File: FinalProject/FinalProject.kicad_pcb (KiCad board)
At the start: 4 copper layers, 100 x 100 mm, 143 parts, among them J1 GSB4111312HR, J10 Conn_01x02, J2 GSB4111312HR, J3 GSB4111312HR, J5 ARJM11D7-502-AB-EW2, J6 DCJ200-10-A-XX-K_REVA, J7 Conn_01x02, J9 Conn_01x03, Q1 NTTFS5C673NLTAG, Q2 NTTFS5C673NLTAG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

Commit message: having DRC error
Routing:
- net /DN1_D-: vias 1 -> 2
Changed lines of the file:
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@@
+	)
+	(via
+		(at 106.7 107.6)
+		(size 0.2)
+		(drill 0.1)
+		(layers "F.Cu" "B.Cu")
+		(net 101)
 	)
 	(via
@@
 	)
 	(segment
+		(start 81.0625 91)
+		(end 80.406249 91)
+		(width 0.2)
+		(layer "F.Cu")
+		(net 141)
+	)
+	(segment
 		(start 39.2125 67.05)
 		(end 39.2125 66.08)
@@
 		(start 39.2125 66.08)
 		(end 38.4125 65.28)
-		(width 0.2)
-		(layer "F.Cu")
-		(net 141)
-	)
-	(segment
-		(start 81.0625 91)
-		(end 80.406249 91)
 		(width 0.2)
 		(layer "F.Cu")
@@
 	)
 	(segment
+		(start 39.2125 68.245344)
+		(end 40.317156 69.35)
+		(width 0.2)
+		(layer "In2.Cu")
+		(net 141)
+	)
+	(segment
+		(start 68.517156 94)
+		(end 74.082844 94)
+		(width 0.2)
+		(layer "In2.Cu")
+		(net 141)
+	)
+	(segment
+		(start 77.132844 90.95)
+		(end 80.05 90.95)
+		(width 0.2)
+		(layer "In2.Cu")
+		(net 141)
+	)
+	(segment
+		(start 74.082844 94)
+		(end 77.132844 90.95)
+		(width 0.2)
+		(layer "In2.Cu")
+		(net 141)
+	)
+	(segment
+		(start 39.2125 67.05)
+		(end 39.2125 68.245344)
+		(width 0.2)
+		(layer "In2.Cu")
+		(net 141)
+	)
+	(segment
+		(start 43.867156 69.35)
+		(end 68.517156 94)
+		(width 0.2)
+		(layer "In2.Cu")
+		(net 141)
+	)
+	(segment
 		(start 40.317156 69.35)
-		(end 39.2125 68.245344)
-		(width 0.2)
-		(layer "In2.Cu")
-		(net 141)
-	)
-	(segment
-		(start 68.517156 94)
 		(end 43.867156 69.35)
-		(width 0.2)
-		(layer "In2.Cu")
-		(net 141)
-	)
-	(segment
-		(start 77.132844 90.95)
-		(end 74.082844 94)
-		(width 0.2)
-		(layer "In2.Cu")
-		(net 141)
-	)
-	(segment
-		(start 80.05 90.95)
-		(end 77.132844 90.95)
-		(width 0.2)
-		(layer "In2.Cu")
-		(net 141)
-	)
-	(segment
-		(start 74.082844 94)
-		(end 68.517156 94)
-		(width 0.2)
-		(layer "In2.Cu")
-		(net 141)
-	)
-	(segment
-		(start 39.2125 68.245344)
-		(end 39.2125 67.05)
-		(width 0.2)
-		(layer "In2.Cu")
-		(net 141)
-	)
-	(segment
-		(start 43.867156 69.35)
-		(end 40.317156 69.35)
 		(width 0.2)
 		(layer "In2.Cu")
@@
 	)
 	(segment
+		(start 45.2125 66.08)
+		(end 45.2125 67.05)
+		(width 0.2)
+		(layer "F.Cu")
+		(net 144)
+	)
+	(segment
 		(start 80.406249 89.5)
 		(end 80.356249 89.45)
@@
 	)
 	(segment
-		(start 45.2125 67.05)
+		(start 44.4125 65.28)
 		(end 45.2125 66.08)
-		(width 0.2)
-		(layer "F.Cu")
-		(net 144)
-	)
-	(segment
-		(start 45.2125 66.08)
-		(end 44.4125 65.28)
 		(width 0.2)
 		(layer "F.Cu")
@@
 	)
 	(segment
+		(start 79.182844 89.45)
+		(end 80.1 89.45)
+		(width 0.2)
+		(layer "In2.Cu")
+		(net 144)
+	)
+	(segment
+		(start 78.75413 89.878714)
+		(end 79.182844 89.45)
+		(width 0.2)
+		(layer "In2.Cu")
+		(net 144)
+	)
+	(segment
+		(start 77.49587 89.878714)
+		(end 78.75413 89.878714)
+		(width 0.2)
+		(layer "In2.Cu")
+		(net 144)
+	)
+	(segment
+		(start 73.667156 86.05)
+		(end 77.49587 89.878714)
+		(width 0.2)
+		(layer "In2.Cu")
+		(net 144)
+	)
+	(segment
 		(start 45.2125 67.545344)
 		(end 63.717156 86.05)
@@
 	)
 	(segment
-		(start 73.667156 86.05)
-		(end 77.49587 89.878714)
-		(width 0.2)
-		(layer "In2.Cu")
-		(net 144)
-	)
-	(segment
-		(start 78.75413 89.878714)
-		(end 79.182844 89.45)
-		(width 0.2)
-		(layer "In2.Cu")
-		(net 144)
-	)
-	(segment
-		(start 77.49587 89.878714)
-		(end 78.75413 89.878714)
-		(width 0.2)
-		(layer "In2.Cu")
-		(net 144)
-	)
-	(segment
-		(start 79.182844 89.45)
-		(end 80.1 89.45)
+		(start 45.2125 67.05)
+		(end 45.2125 67.545344)
 		(width 0.2)
 		(layer "In2.Cu")
@@
 		(width 0.2)
 		(layer "In2.Cu")
-		(net 144)
-	)
-	(segment
-		(start 45.2125 67.05)
-		(end 45.2125 67.545344)
-		(width 0.2)
-		(layer "In2.Cu")

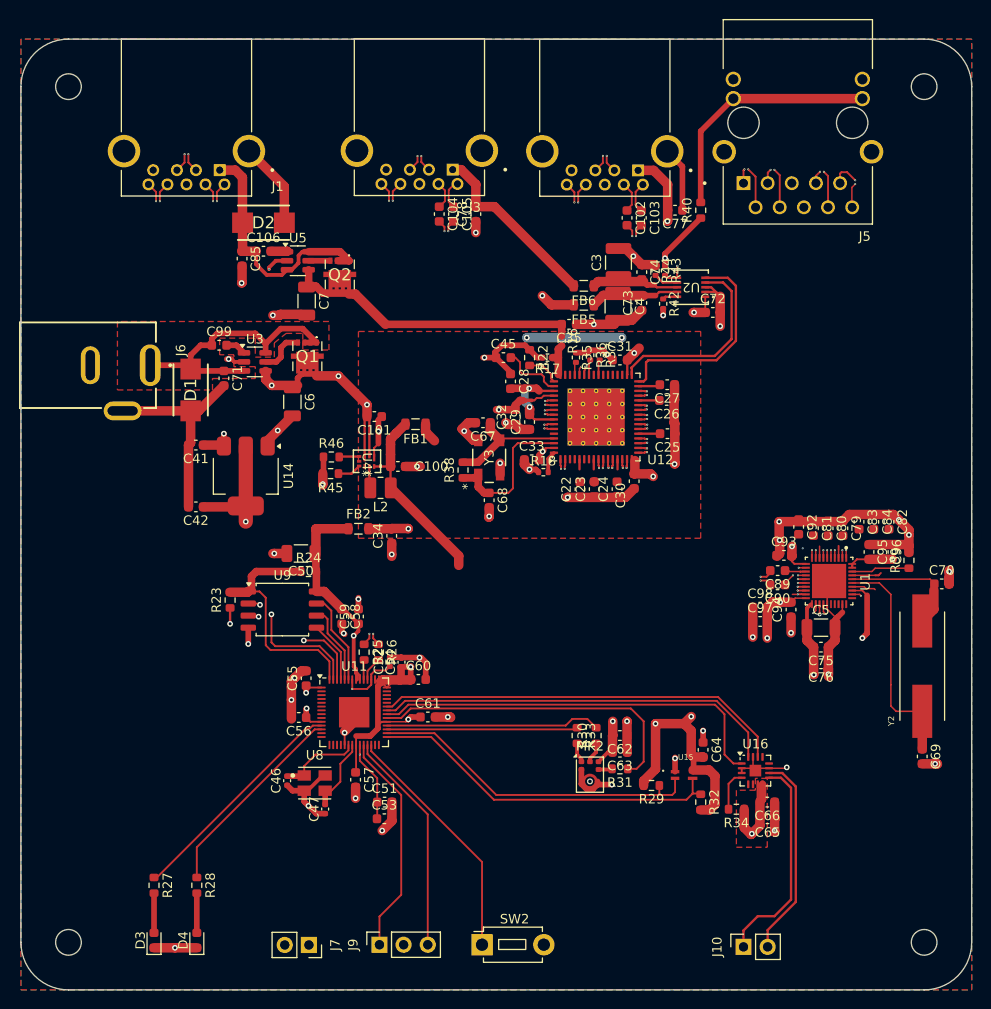
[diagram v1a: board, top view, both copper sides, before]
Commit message: fix vias error
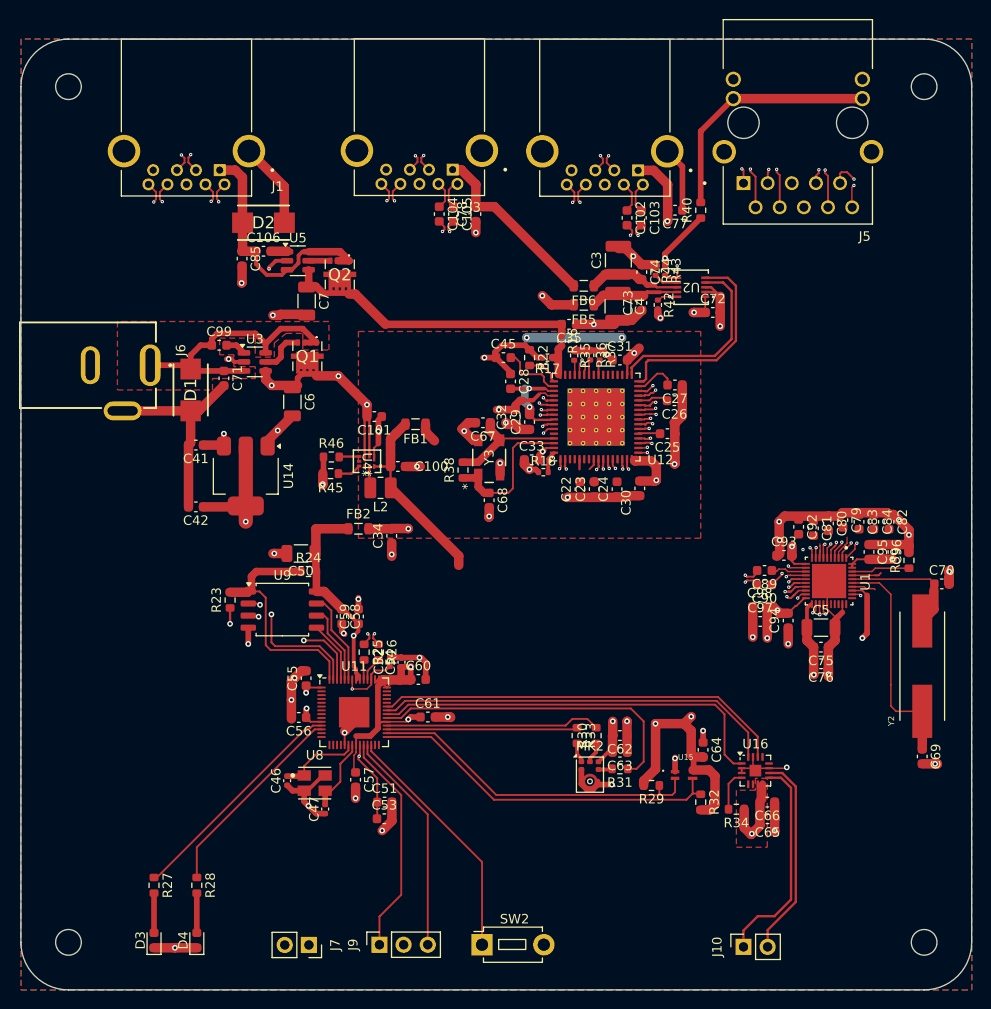
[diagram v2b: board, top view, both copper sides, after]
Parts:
- moved C89 1.38 mm to (103.2, 105.9)
- moved C90 1.38 mm to (103.2, 107.4)
- moved C94 1.20 mm to (105.7, 111.2)
- moved C30 0.96 mm to (90.1, 97.3)
- moved C79 0.87 mm to (111.5, 100.6)
- moved C26 0.81 mm to (93.7, 88.0)
- moved C27 0.81 mm to (93.8, 86.4)
- moved R42 0.57 mm to (92.0, 78.0)
- moved C80 0.51 mm to (109.9, 100.9)
- moved R35 0.29 mm to (83.2, 83.3)
- moved C3 0.24 mm to (87.8, 73.3)
- moved C98 0.07 mm to (102.7, 109.7)
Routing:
- net /DN1_RXN: track 36.0 -> 25.4 mm
- net /USB HUB/USB_FB_3.3V: track 20.4 -> 26.0 mm
- net Net-(U1-U3SSTXN): track 3.54 -> 6.22 mm
- net /USB HUB/USB_FB_1.1V: track 32.4 -> 34.7 mm
- net Net-(U2-OUT1): track 9.34 -> 11.2 mm
- net /DN3_TXP: track 41.7 -> 43.2 mm
- net (no net): track 1.49 -> 0.00 mm
- net Net-(U1-U3SSTXP): track 2.15 -> 3.44 mm
- net +1V1: track 42.3 -> 41.1 mm
- net /DN1_D+: track 29.1 -> 30.2 mm
- net /TD1+: track 88.6 -> 89.7 mm
- net /DN1_TXP: track 23.4 -> 22.3 mm
- net /DN1_TXN: track 22.7 -> 21.7 mm
- net GND: track 228.5 -> 229.5 mm
- net /TD1-: track 90.1 -> 91.0 mm
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
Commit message: increase via hole diameter
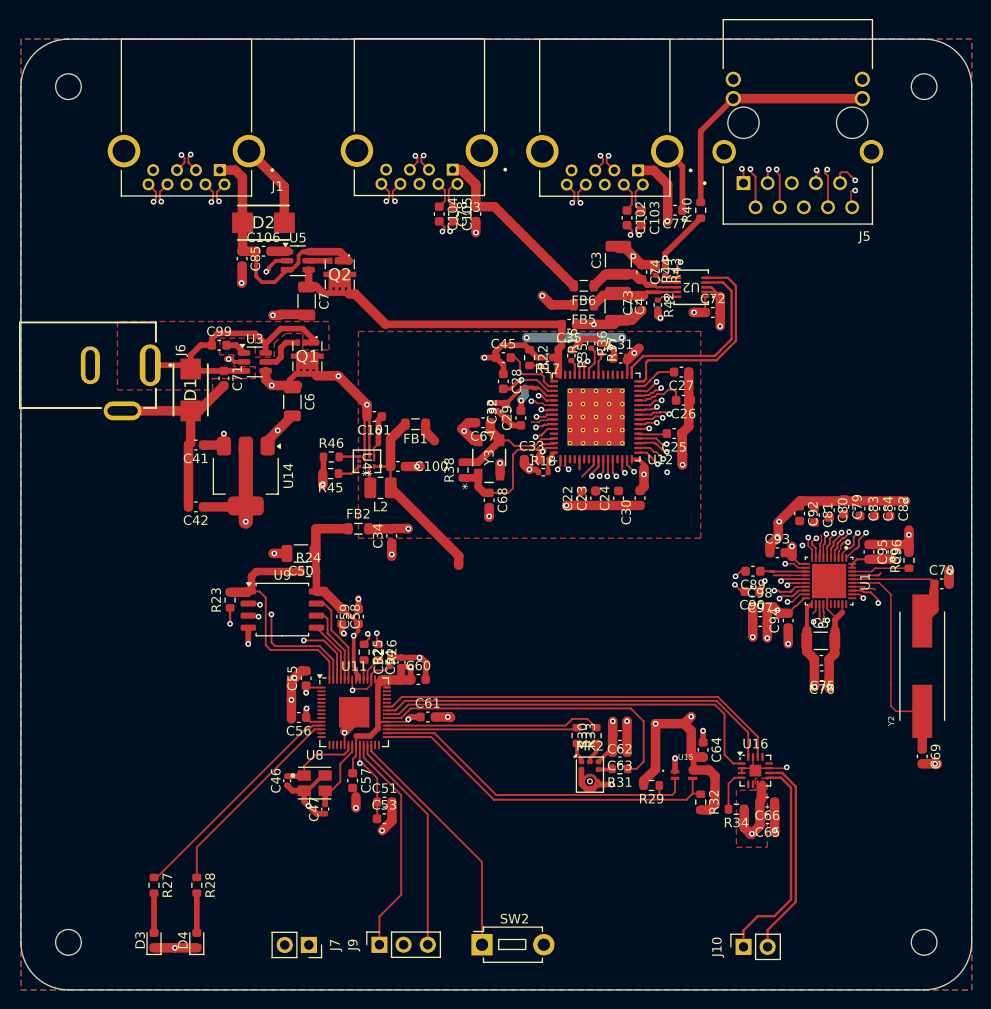
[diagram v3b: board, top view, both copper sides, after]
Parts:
- moved C27 1.52 mm to (94.5, 85.0)
- moved C90 1.48 mm to (101.9, 108.1)
- moved C82 1.40 mm to (116.4, 99.4)
- moved C83 1.40 mm to (113.2, 99.4)
- moved C84 1.40 mm to (114.8, 99.4)
- moved C81 1.40 mm to (108.5, 100.1)
- moved C92 1.40 mm to (106.9, 99.9)
- moved C79 1.40 mm to (111.5, 99.2)
- moved C80 1.40 mm to (110.0, 99.6)
- moved C75 1.39 mm to (109.2, 115.3)
- moved C5 1.39 mm to (109.1, 113.3)
- moved C76 1.27 mm to (109.2, 117.0)
- moved R36 1.24 mm to (85.0, 82.0)
- moved C89 1.22 mm to (102.0, 106.0)
- moved C32 1.17 mm to (76.0, 89.2)
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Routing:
- net +1V1: track 41.1 -> 55.0 mm
- net /DN1_RXP: track 37.5 -> 26.6 mm
- net GND: track 229.5 -> 235.4 mm, vias 50 -> 51
- net /USB HUB/USB_FB_1.1V: track 34.7 -> 40.0 mm
- net /USB HUB/USB_FB_3.3V: track 26.0 -> 21.9 mm
- net /USB HUB/OVERCUR3: track 20.0 -> 22.0 mm
- net /DN3_TXP: track 43.2 -> 41.2 mm
- net +5V: track 52.6 -> 54.6 mm
- net Net-(U1-U3SSTXP): track 3.44 -> 5.28 mm
- net Net-(U12-GANGED/SMBA2/HS_UP): track 1.61 -> 3.30 mm
- net +3.3V: track 132.4 -> 130.9 mm
- net /UP_VBUS: track 26.0 -> 27.4 mm
- net /DN2_D+: track 68.4 -> 69.5 mm
- net /TD4+: track 53.2 -> 54.3 mm
- net /DN1_TXN: track 21.7 -> 20.6 mm
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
